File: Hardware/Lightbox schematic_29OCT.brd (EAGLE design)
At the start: 53.3 x 69.5 mm, 8 parts, among them IC2 7805T, U1 ARDUINOR3-DIMENSION

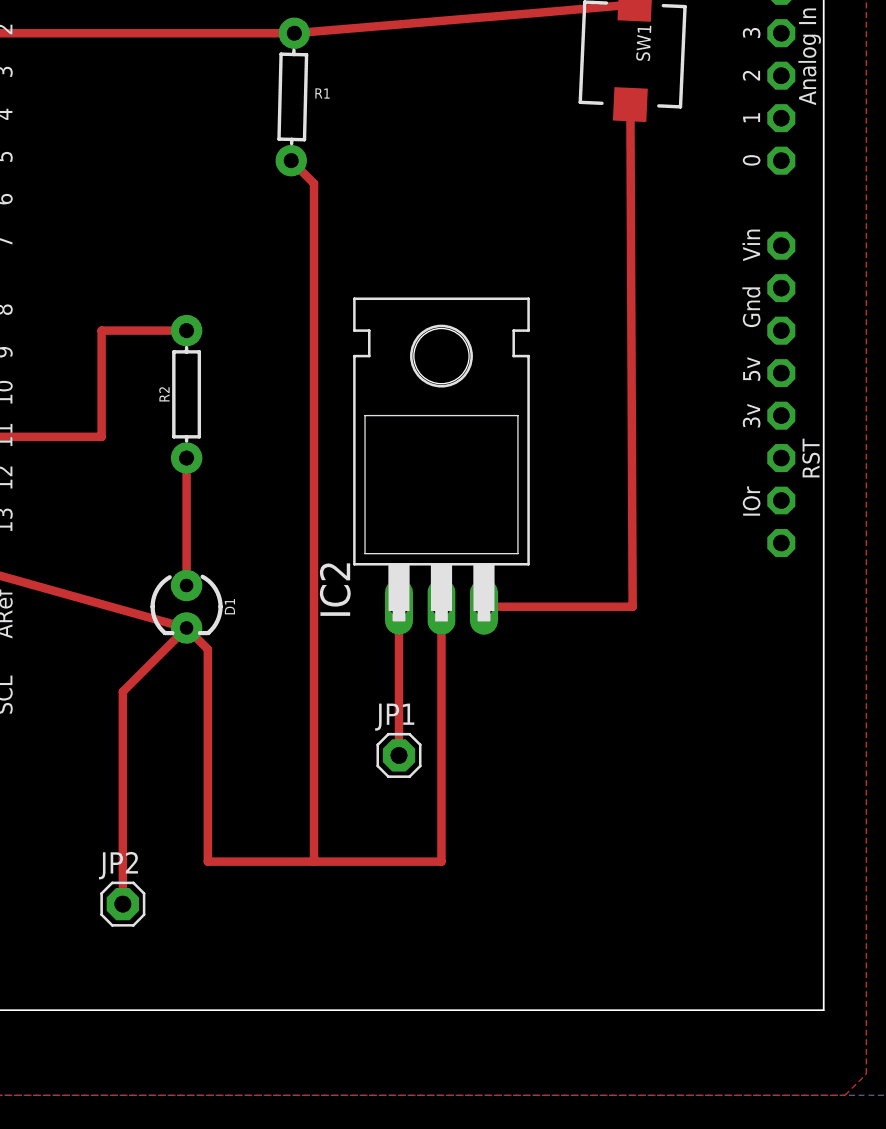
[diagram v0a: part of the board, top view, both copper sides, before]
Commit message: add revs of schematic/PCB iterated on in office
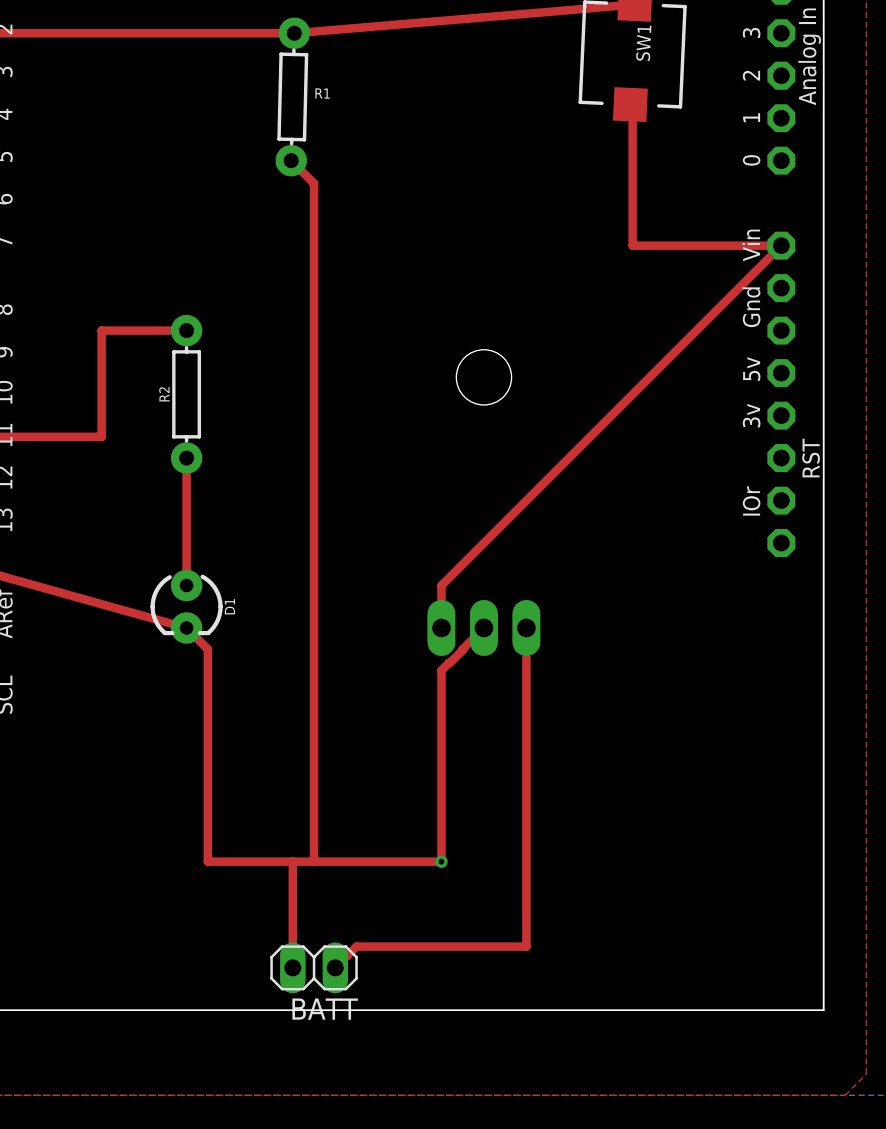
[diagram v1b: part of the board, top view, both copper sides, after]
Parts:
- removed JP1, JP2: (no value), adafruit:1X01
- added BATT: (no value), pinhead:1X02
- moved IC2 2.84 mm to (81.3, 38.1), flipped to the bottom
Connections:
- removed net N$1: IC2.1, JP1.1
- removed net VIN: U1.VIN
- new net BATT: BATT.1, IC2.1
- net +5V: now also U1.VIN
- net GND: now also BATT.2; no longer JP2.1
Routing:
- net BATT: track 0.00 -> 31.0 mm
- net GND: track 118.9 -> 107.0 mm, vias 0 -> 1
- net +5V: track 38.9 -> 48.7 mm
- net N$1: track 8.89 -> 0.00 mm
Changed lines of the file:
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@@
 <?xml version="1.0" encoding="utf-8"?>
 <!DOCTYPE eagle SYSTEM "eagle.dtd">
-<eagle version="9.2.0">
+<eagle version="9.2.2">
 <drawing>
 <settings>
@@
 </autorouter>
 <elements>
-<element name="IC2" library="linear" library_urn="urn:adsk.eagle:library:262" package="TO220H" package3d_urn="urn:adsk.eagle:package:16414/1" value="7805T" x="78.74" y="39.37">
-<attribute name="NAME" x="73.279" y="28.448" size="1.778" layer="25" ratio="10" rot="R90"/>
-<attribute name="VALUE" x="86.106" y="28.321" size="1.778" layer="27" ratio="10" rot="R90"/>
-</element>
-<element name="R1" library="SparkFun-Resistors" library_urn="urn:adsk.eagle:library:532" package="AXIAL-0.3" package3d_urn="urn:adsk.eagle:package:39658/1" value="100k" x="69.85" y="59.69" rot="R88.6">
+<element name="IC2" library="linear" library_urn="urn:adsk.eagle:library:262" package="TO220H" package3d_urn="urn:adsk.eagle:package:16414/1" value="7805T" x="81.28" y="38.1" smashed="yes" rot="MR0">
+<attribute name="NAME" x="86.741" y="27.178" size="1.778" layer="26" ratio="10" rot="MR90"/>
+<attribute name="VALUE" x="73.914" y="27.051" size="1.778" layer="28" ratio="10" rot="MR90"/>
+</element>
+<element name="R1" library="SparkFun-Resistors" library_urn="urn:adsk.eagle:library:532" package="AXIAL-0.3" package3d_urn="urn:adsk.eagle:package:39658/1" value="100k" x="69.85" y="59.69" smashed="yes" rot="R88.6">
 <attribute name="NAME" x="71.632121875" y="60.2013625" size="0.6096" layer="25" font="vector" ratio="20" rot="R179.1" align="bottom-center"/>
 <attribute name="PROD_ID" value="RES-12184" x="69.85" y="59.69" size="1.778" layer="27" rot="R88.6" display="off"/>
 <attribute name="VALUE" x="67.216396875" y="60.760025" size="0.6096" layer="27" font="vector" ratio="20" rot="R345.2" align="top-center"/>
 </element>
-<element name="D1" library="SparkFun-LED" library_urn="urn:adsk.eagle:library:529" package="LED_3MM" package3d_urn="urn:adsk.eagle:package:39361/1" value="" x="63.5" y="29.21" rot="R270">
+<element name="D1" library="SparkFun-LED" library_urn="urn:adsk.eagle:library:529" package="LED_3MM" package3d_urn="urn:adsk.eagle:package:39361/1" value="" x="63.5" y="29.21" smashed="yes" rot="R270">
 <attribute name="NAME" x="65.786" y="29.21" size="0.6096" layer="25" font="vector" ratio="20" rot="R270" align="bottom-center"/>
 <attribute name="PROD_ID" value="DIO-08794" x="63.5" y="29.21" size="1.778" layer="27" rot="R270" display="off"/>
 <attribute name="VALUE" x="61.214" y="29.21" size="0.6096" layer="27" font="vector" ratio="20" rot="R270" align="top-center"/>
 </element>
-<element name="U1" library="adafruit" library_urn="urn:adsk.eagle:library:420" package="ARDUINOR3" package3d_urn="urn:adsk.eagle:package:6240877/1" value="ARDUINOR3-DIMENSION" x="101.6" y="5.08" rot="R90"/>
-<element name="R2" library="SparkFun-Resistors" library_urn="urn:adsk.eagle:library:532" package="AXIAL-0.3" package3d_urn="urn:adsk.eagle:package:39658/1" value="100k" x="63.5" y="41.91" rot="R90">
+<element name="U1" library="adafruit" library_urn="urn:adsk.eagle:library:420" package="ARDUINOR3" package3d_urn="urn:adsk.eagle:package:6240877/1" value="ARDUINOR3-DIMENSION" x="101.6" y="5.08" smashed="yes" rot="R90"/>
+<element name="R2" library="SparkFun-Resistors" library_urn="urn:adsk.eagle:library:532" package="AXIAL-0.3" package3d_urn="urn:adsk.eagle:package:39658/1" value="100k" x="63.5" y="41.91" smashed="yes" rot="R90">
 <attribute name="NAME" x="62.484" y="41.91" size="0.6096" layer="25" font="vector" ratio="20" rot="R90" align="bottom-center"/>
 <attribute name="PROD_ID" value="RES-12184" x="63.5" y="41.91" size="1.778" layer="27" rot="R90" display="off"/>
 <attribute name="VALUE" x="65.65256875" y="41.343325" size="0.6096" layer="27" font="vector" ratio="20" rot="R117.7" align="top-center"/>
 </element>
-<element name="SW1" library="adafruit" library_urn="urn:adsk.eagle:library:420" package="PUSHBUTTON_SMD_SJ" package3d_urn="urn:adsk.eagle:package:6240956/1" value="" x="90.17" y="62.23" rot="R87.4">
+<element name="SW1" library="adafruit" library_urn="urn:adsk.eagle:library:420" package="PUSHBUTTON_SMD_SJ" package3d_urn="urn:adsk.eagle:package:6240956/1" value="" x="90.17" y="62.23" smashed="yes" rot="R87.4">
 <attribute name="NAME" x="91.191959375" y="61.768853125" size="0.8128" layer="25" ratio="18" rot="R87.4"/>
 <attribute name="VALUE" x="90.8505625" y="60.4192625" size="0.4064" layer="27" ratio="10" rot="R87.4"/>
 </element>
-<element name="JP1" library="adafruit" library_urn="urn:adsk.eagle:library:420" package="1X01" package3d_urn="urn:adsk.eagle:package:6240654/1" value="" x="76.2" y="20.32">
-<attribute name="NAME" x="74.8538" y="22.1488" size="1.27" layer="25" ratio="10"/>
-<attribute name="VALUE" x="74.93" y="17.145" size="1.27" layer="27"/>
-</element>
-<element name="JP2" library="adafruit" library_urn="urn:adsk.eagle:library:420" package="1X01" package3d_urn="urn:adsk.eagle:package:6240654/1" value="" x="59.69" y="11.43">
-<attribute name="NAME" x="58.3438" y="13.2588" size="1.27" layer="25" ratio="10"/>
-<attribute name="VALUE" x="58.42" y="8.255" size="1.27" layer="27"/>
+<element name="BATT" library="pinhead" library_urn="urn:adsk.eagle:library:325" package="1X02" package3d_urn="urn:adsk.eagle:package:22435/2" value="" x="71.12" y="7.62" smashed="yes" rot="R180">
+<attribute name="NAME" x="73.7362" y="5.7912" size="1.27" layer="25" ratio="10" rot="R180"/>
+<attribute name="VALUE" x="73.66" y="10.795" size="1.27" layer="27" rot="R180"/>
 </element>
 </elements>
 <signals>
-<signal name="N$1">
+<signal name="BATT">
 <contactref element="IC2" pad="1"/>
-<contactref element="JP1" pad="1"/>
-<wire x1="76.2" y1="29.21" x2="76.2" y2="20.32" width="0.508" layer="1"/>
-</signal>
-<signal name="VIN">
-<contactref element="U1" pad="VIN"/>
+<contactref element="BATT" pad="1"/>
+<wire x1="72.39" y1="7.62" x2="73.66" y2="8.89" width="0.508" layer="1"/>
+<wire x1="73.66" y1="8.89" x2="83.82" y2="8.89" width="0.508" layer="1"/>
+<wire x1="83.82" y1="8.89" x2="83.82" y2="27.94" width="0.508" layer="1"/>
 </signal>
 <signal name="GND1">
@@
 </polygon>
 <wire x1="49.3522" y1="31.496" x2="50.8" y2="31.496" width="0.1524" layer="16"/>
-<contactref element="JP2" pad="1"/>
 <wire x1="63.5" y1="27.94" x2="50.8" y2="31.496" width="0.508" layer="1"/>
-<wire x1="63.5" y1="27.94" x2="59.69" y2="24.13" width="0.508" layer="1"/>
-<wire x1="59.69" y1="24.13" x2="59.69" y2="11.43" width="0.508" layer="1"/>
 <wire x1="63.5" y1="27.94" x2="64.77" y2="26.67" width="0.508" layer="1"/>
 <wire x1="64.77" y1="26.67" x2="64.77" y2="13.97" width="0.508" layer="1"/>
-<wire x1="64.77" y1="13.97" x2="71.12" y2="13.97" width="0.508" layer="1"/>
+<wire x1="64.77" y1="13.97" x2="69.85" y2="13.97" width="0.508" layer="1"/>
+<wire x1="69.85" y1="13.97" x2="71.12" y2="13.97" width="0.508" layer="1"/>
 <wire x1="71.12" y1="13.97" x2="78.74" y2="13.97" width="0.508" layer="1"/>
-<wire x1="78.74" y1="13.97" x2="78.74" y2="29.21" width="0.508" layer="1"/>
 <wire x1="69.7569125" y1="55.881134375" x2="71.12" y2="54.518046875" width="0.508" layer="1"/>
 <wire x1="71.12" y1="54.518046875" x2="71.12" y2="13.97" width="0.508" layer="1"/>
+<contactref element="BATT" pad="2"/>
+<via x="78.74" y="13.97" extent="1-16" drill="0.35"/>
+<wire x1="78.74" y1="25.4" x2="78.74" y2="13.97" width="0.508" layer="1"/>
+<wire x1="81.28" y1="27.94" x2="79.9846" y2="26.6446" width="0.508" layer="1"/>
+<wire x1="79.9846" y1="26.6446" x2="79.9846" y2="26.58626875" width="0.508" layer="1"/>
+<wire x1="79.9846" y1="26.58626875" x2="79.25553125" y2="25.8572" width="0.508" layer="1"/>
+<wire x1="79.25553125" y1="25.8572" x2="79.1972" y2="25.8572" width="0.508" layer="1"/>
+<wire x1="79.1972" y1="25.8572" x2="78.74" y2="25.4" width="0.508" layer="1"/>
+<wire x1="69.85" y1="7.62" x2="69.85" y2="13.97" width="0.508" layer="1"/>
 </signal>
 <signal name="+5V">
 <contactref element="SW1" pad="P$2"/>
 <contactref element="IC2" pad="3"/>
-<wire x1="90.033909375" y1="59.2330875" x2="90.17" y2="29.21" width="0.508" layer="1"/>
-<wire x1="90.17" y1="29.21" x2="81.28" y2="29.21" width="0.508" layer="1"/>
+<contactref element="U1" pad="VIN"/>
+<wire x1="99.06" y1="50.8" x2="78.74" y2="30.48" width="0.508" layer="1"/>
+<wire x1="78.74" y1="30.48" x2="78.74" y2="27.94" width="0.508" layer="1"/>
+<wire x1="99.06" y1="50.8" x2="90.17" y2="50.8" width="0.508" layer="1"/>
+<wire x1="90.17" y1="50.8" x2="90.17" y2="59.096996875" width="0.508" layer="1"/>
+<wire x1="90.17" y1="59.096996875" x2="90.033909375" y2="59.2330875" width="0.508" layer="1"/>
 </signal>
 <signal name="5V">
